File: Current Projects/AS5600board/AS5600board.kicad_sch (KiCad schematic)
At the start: 1 part, among them U1 AS5600

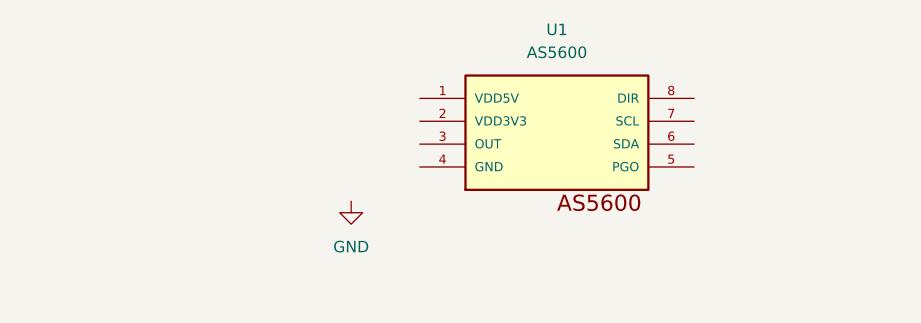
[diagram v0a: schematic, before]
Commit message: First full schematic of AS5600
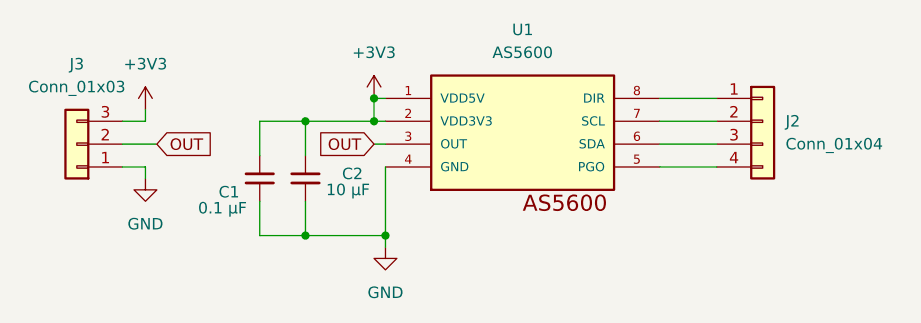
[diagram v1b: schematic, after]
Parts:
- added C1: 0.1 µF, Package_SO:SOIC-8_3.9x4.9mm_P1.27mm, symbol Device:C_Small
- added C2: 10 µF, Package_SO:SOIC-8_3.9x4.9mm_P1.27mm, symbol Device:C_Small
- added J2: Conn_01x04, Connector_PinHeader_2.54mm:PinHeader_1x04_P2.54mm_Vertical, symbol Connector_Generic:Conn_01x04
- added J3: Conn_01x03, Connector_PinHeader_2.54mm:PinHeader_1x04_P2.54mm_Vertical, symbol Connector_Generic:Conn_01x03
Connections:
- net GND: now also U1.4 (GND), C1.1, C2.2, J3.1 (Pin_1)
- net +3V3: now reaches U1.1 (VDD5V)
- net +3V3: now also U1.2 (VDD3V3), C1.2, C2.1, J3.3 (Pin_3)
- net OUT: now reaches U1.3 (OUT)
- net OUT: now also J3.2 (Pin_2)
- net at U1.5 (PGO): now also J2.4 (Pin_4)
- net at U1.6 (SDA): now also J2.3 (Pin_3)
- net at U1.7 (SCL): now also J2.2 (Pin_2)
- net at U1.8 (DIR): now also J2.1 (Pin_1)
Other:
- moved on the sheet: U1

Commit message: edited pcb layout
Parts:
- C1, C2: footprint Package_SO:SOIC-8_3.9x4.9mm_P1.27mm -> Capacitor_SMD:C_0603_1608Metric_Pad1.08x0.95mm_HandSolder
- J3: footprint Connector_PinHeader_2.54mm:PinHeader_1x04_P2.54mm_Vertical -> Connector_PinHeader_2.54mm:PinHeader_1x03_P2.54mm_Vertical
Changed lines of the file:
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@@
 			)
 		)
-		(property "Footprint" "Package_SO:SOIC-8_3.9x4.9mm_P1.27mm"
+		(property "Footprint" "Capacitor_SMD:C_0603_1608Metric_Pad1.08x0.95mm_HandSolder"
 			(at 92.71 102.87 0)
 			(hide yes)
@@
 			)
 		)
-		(property "Footprint" "Package_SO:SOIC-8_3.9x4.9mm_P1.27mm"
+		(property "Footprint" "Capacitor_SMD:C_0603_1608Metric_Pad1.08x0.95mm_HandSolder"
 			(at 87.63 102.87 0)
 			(hide yes)
@@
 			)
 		)
-		(property "Footprint" "Connector_PinHeader_2.54mm:PinHeader_1x04_P2.54mm_Vertical"
+		(property "Footprint" "Connector_PinHeader_2.54mm:PinHeader_1x03_P2.54mm_Vertical"
 			(at 67.31 99.06 0)
 			(hide yes)
